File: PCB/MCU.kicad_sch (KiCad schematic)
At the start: 5 parts, among them U1 STM32F405RGTx

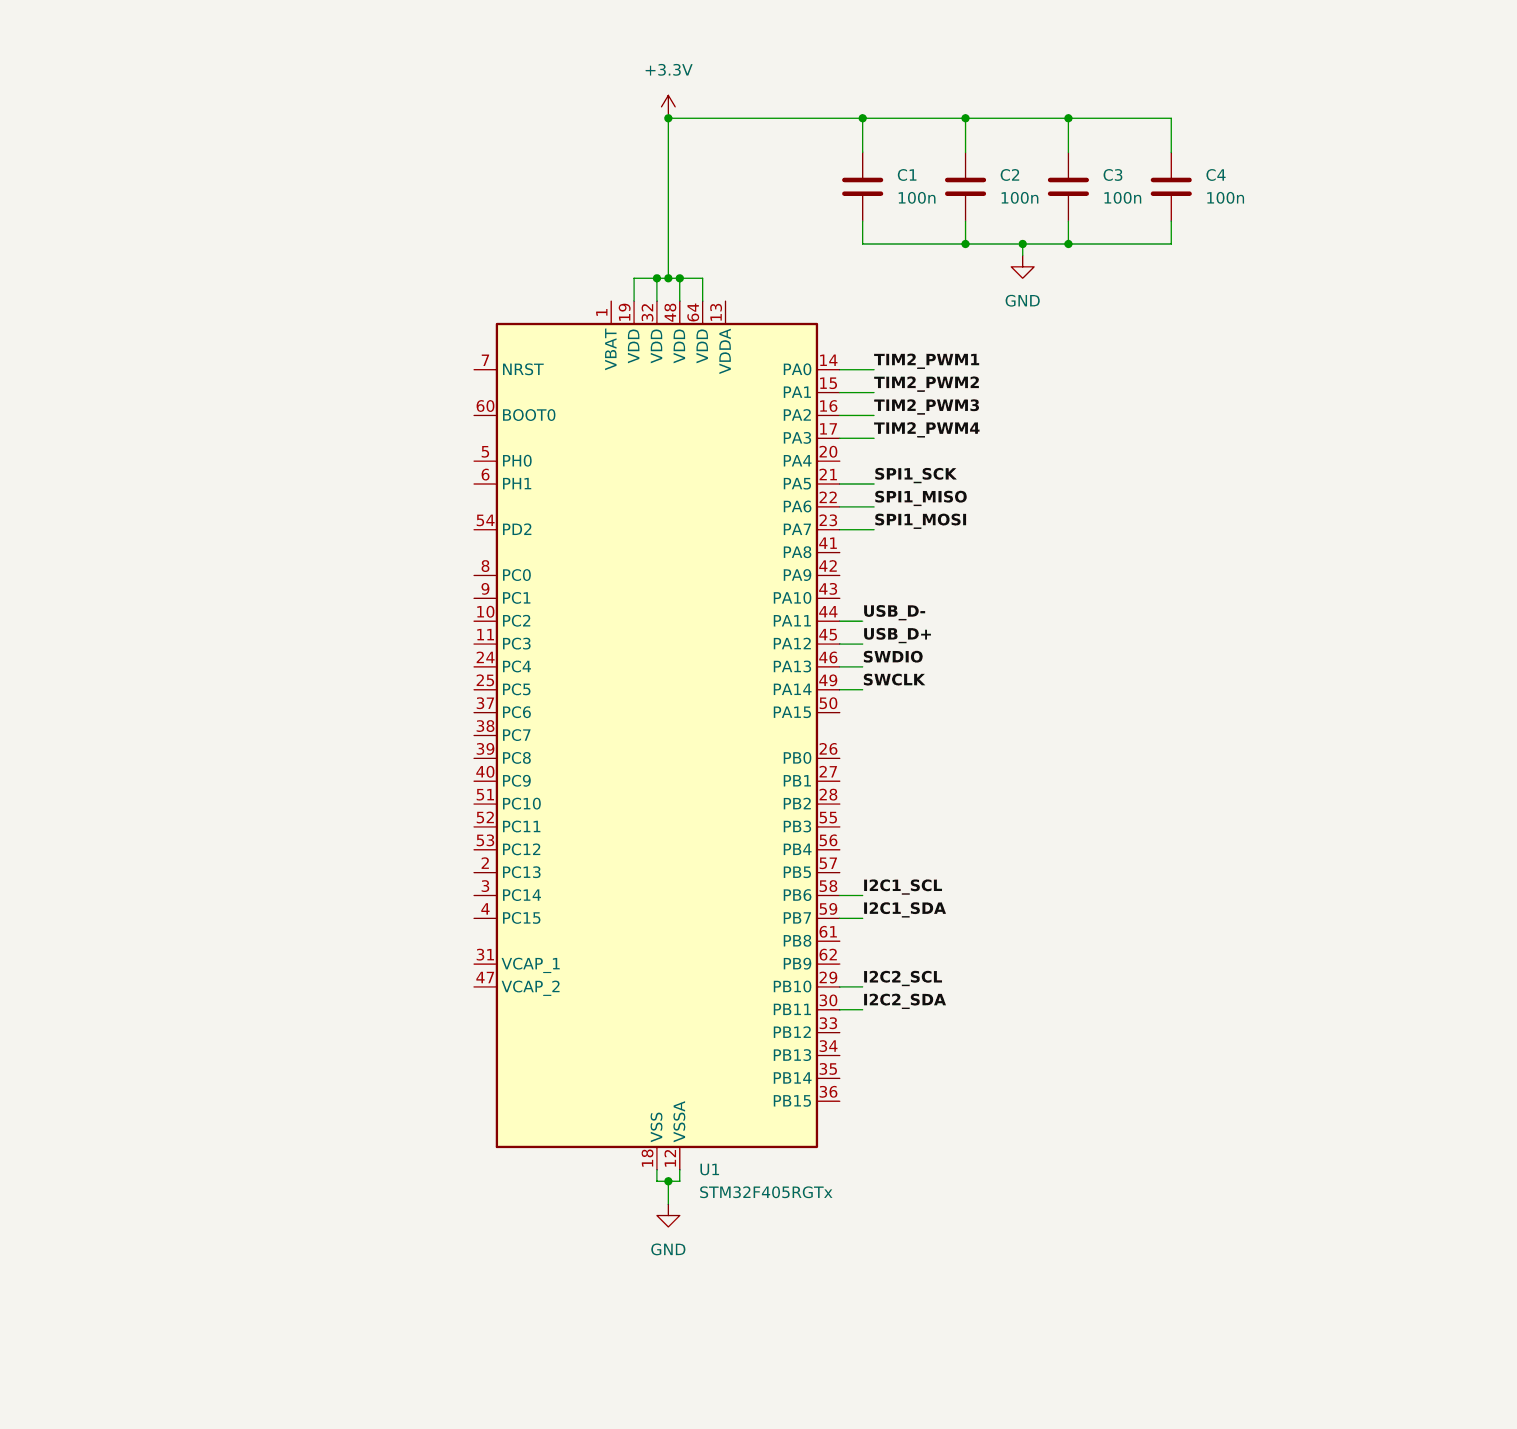
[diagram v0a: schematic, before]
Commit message: Added MCU interfaces and started sensor design
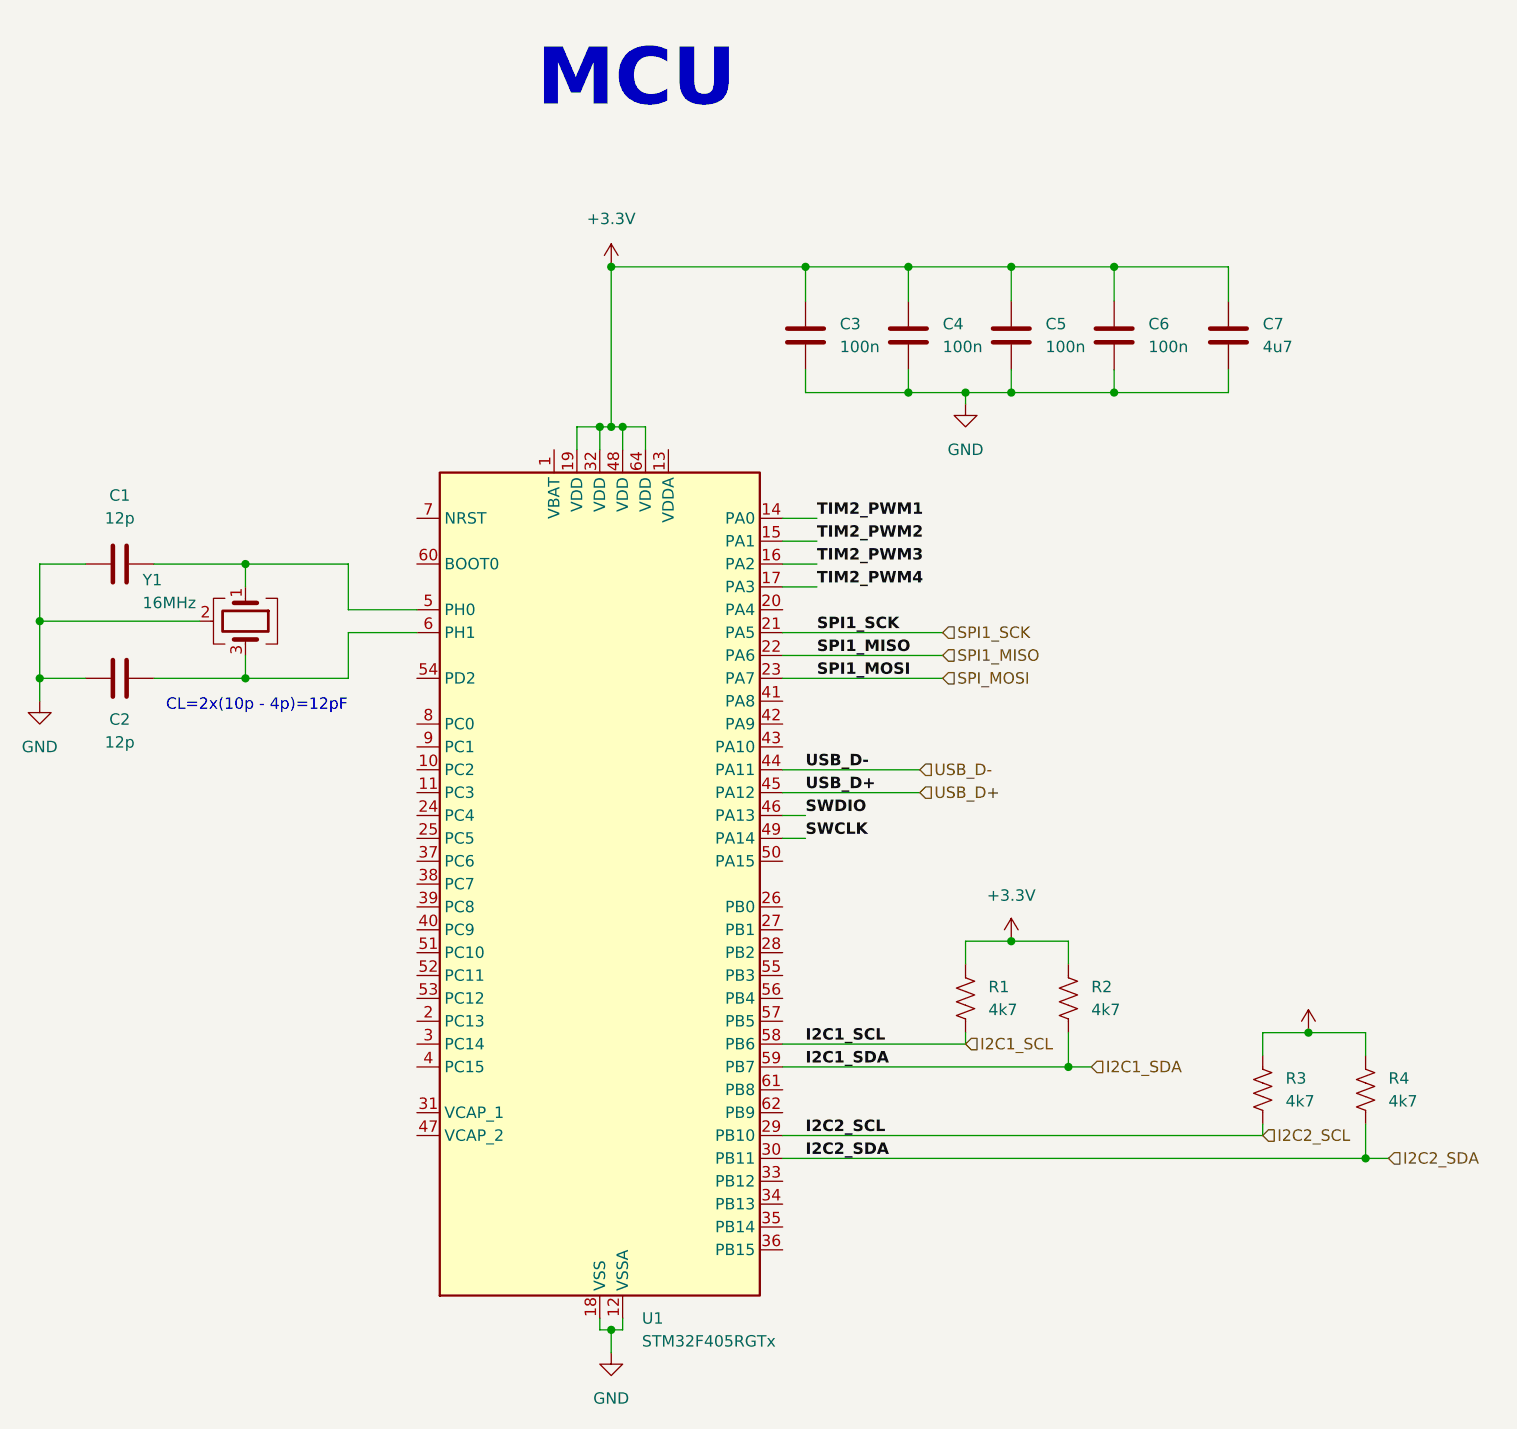
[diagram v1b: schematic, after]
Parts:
- added C1, C2: 12p, symbol Device:C
- added C7: 4u7, symbol Device:C
- added R1, R2, R3, R4: 4k7, PCM_Resistor_SMD_AKL:R_0402_1005Metric, symbol Device:R_US
- added Y1: 16MHz, Crystal:Crystal_SMD_2520-4Pin_2.5x2.0mm, symbol Device:Crystal_GND24
- renumbered C1 to C3, C2 to C4, C3 to C5, C4 to C6
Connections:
- net +3.3V: now also C7.1, R1.1, R2.1, R3.1, R4.1
- net GND: now also C1.1, C2.2, C7.2, Y1.2 (G), Y1.4 (G)
- net I2C1_SCL: now also R1.2
- net I2C1_SDA: now also R2.2
- net I2C2_SCL: now also R3.2
- net I2C2_SDA: now also R4.2
- net at U1.5 (PH0): now also C1.2, Y1.1
- net at U1.6 (PH1): now also C2.1, Y1.3
- net SPI1_MOSI renamed SPI_MOSI
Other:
- note added: "CL=2x(10p - 4p)=12pF"
- note added: "MCU"
- moved on the sheet: C3, C4, C5, C6, U1

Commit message: Slight MCU Interface Change
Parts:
- Y1: value 16MHz -> 24 MHz
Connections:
- net USART6_TX: now reaches U1.37 (PC6)
- net USART6_RX: now reaches U1.38 (PC7)
- net USART1_TX: now reaches U1.42 (PA9)
- net USART1_RX: now reaches U1.43 (PA10)
- net USART3_TX: now reaches U1.51 (PC10)
- net USART3_RX: now reaches U1.52 (PC11)
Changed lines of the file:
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@@
+	(wire
+		(pts
+			(xy 153.67 97.79) (xy 170.18 97.79)
+		)
+		(stroke
+			(width 0)
+			(type default)
+		)
+	)
 	(wire
 		(pts
@@
 	(wire
 		(pts
+			(xy 97.79 120.65) (xy 113.03 120.65)
+		)
+		(stroke
+			(width 0)
+			(type default)
+		)
+	)
+	(wire
+		(pts
 			(xy 133.35 162.56) (xy 133.35 161.29)
 		)
@@
 	(wire
 		(pts
+			(xy 99.06 110.49) (xy 113.03 110.49)
+		)
+		(stroke
+			(width 0)
+			(type default)
+		)
+	)
+	(wire
+		(pts
 			(xy 133.35 62.23) (xy 133.35 64.77)
 		)
@@
 	(wire
 		(pts
+			(xy 153.67 95.25) (xy 170.18 95.25)
+		)
+		(stroke
+			(width 0)
+			(type default)
+		)
+	)
+	(wire
+		(pts
 			(xy 138.43 62.23) (xy 138.43 64.77)
 		)
@@
 	(wire
 		(pts
+			(xy 97.79 123.19) (xy 113.03 123.19)
+		)
+		(stroke
+			(width 0)
+			(type default)
+		)
+	)
+	(wire
+		(pts
 			(xy 173.99 119.38) (xy 179.07 119.38)
 		)
@@
 		(pts
 			(xy 105.41 85.09) (xy 113.03 85.09)
+		)
+		(stroke
+			(width 0)
+			(type default)
+		)
+	)
+	(wire
+		(pts
+			(xy 99.06 113.03) (xy 113.03 113.03)
 		)
 		(stroke
@@
 		)
 	)
+	(label "USART1_TX"
+		(at 156.21 95.25 0)
+		(effects
+			(font
+				(size 1.27 1.27)
+			)
+			(justify left bottom)
+		)
+	)
+	(label "USART3_TX"
+		(at 110.49 120.65 180)
+		(effects
+			(font
+				(size 1.27 1.27)
+			)
+			(justify right bottom)
+		)
+	)
+	(label "USART6_TX"
+		(at 110.49 110.49 180)
+		(effects
+			(font
+				(size 1.27 1.27)
+			)
+			(justify right bottom)
+		)
+	)
+	(label "USART3_RX"
+		(at 110.49 123.19 180)
+		(effects
+			(font
+				(size 1.27 1.27)
+			)
+			(justify right bottom)
+		)
+	)
 	(label "SPI1_MOSI"
 		(at 157.48 90.17 0)
@@
 		)
 	)
+	(label "USART6_RX"
+		(at 110.49 113.03 180)
+		(effects
+			(font
+				(size 1.27 1.27)
+			)
+			(justify right bottom)
+		)
+	)
 	(label "TIM2_PWM1"
 		(at 157.48 72.39 0)
@@
 				(thickness 0.254)
 				(bold yes)
+			)
+			(justify left bottom)
+		)
+	)
+	(label "USART1_RX"
+		(at 156.21 97.79 0)
+		(effects
+			(font
+				(size 1.27 1.27)
 			)
 			(justify left bottom)
@@
 		)
 	)
+	(hierarchical_label "USART1_RX"
+		(shape input)
+		(at 170.18 97.79 0)
+		(effects
+			(font
+				(size 1.27 1.27)
+			)
+			(justify left)
+		)
+	)
 	(hierarchical_label "USB_D-"
 		(shape input)
@@
 		)
 	)
+	(hierarchical_label "USART6_RX"
+		(shape input)
+		(at 99.06 113.03 180)
+		(effects
+			(font
+				(size 1.27 1.27)
+			)
+			(justify right)
+		)
+	)
 	(hierarchical_label "SPI1_SCK"
 		(shape input)
@@
 		)
 	)
+	(hierarchical_label "USART6_TX"
+		(shape input)
+		(at 99.06 110.49 180)
+		(effects
+			(font
+				(size 1.27 1.27)
+			)
+			(justify right)
+		)
+	)
 	(hierarchical_label "I2C1_SDA"
 		(shape input)
@@
 		)
 	)
+	(hierarchical_label "USART3_RX"
+		(shape input)
+		(at 97.79 123.19 180)
+		(effects
+			(font
+				(size 1.27 1.27)
+			)
+			(justify right)
+		)
+	)
+	(hierarchical_label "USART3_TX"
+		(shape input)
+		(at 97.79 120.65 180)
+		(effects
+			(font
+				(size 1.27 1.27)
+			)
+			(justify right)
+		)
+	)
 	(hierarchical_label "I2C2_SCL"
 		(shape input)
@@
 		(shape input)
 		(at 171.45 90.17 0)
+		(effects
+			(font
+				(size 1.27 1.27)
+			)
+			(justify left)
+		)
+	)
+	(hierarchical_label "USART1_TX"
+		(shape input)
+		(at 170.18 95.25 0)
 		(effects
 			(font
@@
 			)
 		)
-		(property "Value" "16MHz"
-			(at 82.55 81.788 90)
-			(show_name no)
-			(do_not_autoplace no)
+		(property "Value" "24 MHz"
+			(at 81.28 81.788 90)
+			(show_name no)
+			(do_not_autoplace no)
